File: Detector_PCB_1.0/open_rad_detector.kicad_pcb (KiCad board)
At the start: 2 copper layers, 48.1 x 120.3 mm, 23 parts, among them IC1 LM3914V, J1 Outer_Shield, J2 Electrode, J3 Batt, Q1 FMMT734, Q2 FMMT734, SW1 POWER, SW2 BUZZER, U1 LD1117S50TR_SOT223, U2 MCP6N11

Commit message: Added LEDs
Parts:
- added D10: LED, LEDs:LED_1206, F.Cu at (154.3, 114.6)
- added D11: LED, LEDs:LED_1206, F.Cu at (160.3, 109.1)
- added D3: LED, LEDs:LED_1206, F.Cu at (142.4, 109.1)
- added D4: LED, LEDs:LED_1206, F.Cu at (142.4, 114.6)
- added D5: LED, LEDs:LED_1206, F.Cu at (148.4, 109.1)
- added D6: LED, LEDs:LED_1206, F.Cu at (142.4, 120.2)
- added D7: LED, LEDs:LED_1206, F.Cu at (148.4, 114.6)
- added D8: LED, LEDs:LED_1206, F.Cu at (154.3, 109.1)
- added D9: LED, LEDs:LED_1206, F.Cu at (148.4, 120.2)
- RV1: footprint Potentiometers:Potentiometer_Trimmer_Piher_PT-10v10_Horizontal_Px10.0mm_Py5.0mm_MountLS -> Potentiometers:Potentiometer_Trimmer_Piher_PT-10v10_Horizontal_Px10.0mm_Py5.0mm
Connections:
- BZ1 pad 2: GND -> L10
- IC1 pad 1: (no net) -> L1
- IC1 pad 10: (no net) -> Net-(IC1-Pad10)
- IC1 pad 11: (no net) -> +BATT
- IC1 pad 12: (no net) -> L10
- IC1 pad 13: (no net) -> L9
- IC1 pad 14: (no net) -> L8
- IC1 pad 15: (no net) -> L7
- IC1 pad 16: (no net) -> L6
- IC1 pad 17: (no net) -> L5
- IC1 pad 18: (no net) -> L4
- IC1 pad 19: (no net) -> L3
- IC1 pad 2: (no net) -> GND
- IC1 pad 20: (no net) -> L2
- IC1 pad 3: (no net) -> +BATT
- IC1 pad 4: (no net) -> GND
- IC1 pad 6: (no net) -> Net-(IC1-Pad6)
- IC1 pad 7: (no net) -> Net-(IC1-Pad7)
- IC1 pad 8: (no net) -> Net-(IC1-Pad8)
- IC1 pad 9: (no net) -> Net-(IC1-Pad9)
- J3 pad 1: GND -> Net-(J3-Pad1)
- Q2 pad 1: (no net) -> Net-(Q2-Pad1)
- SW1 pad 1: Net-(J3-Pad2) -> Net-(SW1-Pad1)
- SW2 pad 2: Net-(SW2-Pad2) -> +BATT
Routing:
- net Net-(J3-Pad2): track 43.6 -> 39.2 mm
- net Net-(SW2-Pad2): track 0.65 -> 0.00 mm
- net +BATT: track 122.9 -> 123.6 mm

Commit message: Work in the new version
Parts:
- removed D1: LED, LEDs:LED_1206
- added C5: 10u, Capacitors_SMD:C_1206, F.Cu at (107.4, 147.8)
- added L1: 33u, Inductors_NEOSID:Neosid_Inductor_SM-NE29_SMD1008, F.Cu at (106.4, 151.9)
- added R6: LMR2, Resistors_SMD:R_0805, F.Cu at (117.9, 154.2)
- R4: value R_LED -> LMR1
- moved D8 69.1 mm to (90.0, 134.2), turned to 90 degrees
- moved D5 68.2 mm to (85.0, 134.2), turned to 90 degrees
- moved D3 67.3 mm to (80.0, 134.2), turned to 90 degrees
- moved D10 62.5 mm to (95.0, 134.2), turned to 90 degrees
- moved D11 51.9 mm to (114.9, 134.2), turned to 90 degrees
- moved D4 46.8 mm to (99.9, 134.2), turned to 90 degrees
- moved D9 40.9 mm to (109.9, 134.2), turned to 90 degrees
- moved D6 40.0 mm to (104.9, 134.2), turned to 90 degrees
- moved D7 34.6 mm to (119.9, 134.2), turned to 90 degrees
- moved IC1 24.8 mm to (114.8, 145.0), turned to 90 degrees
- moved R4 23.3 mm to (117.9, 151.9), turned to 0 degrees
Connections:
- D10 pad 2: +BATT -> +12V
- D11 pad 2: +BATT -> +12V
- D3 pad 2: +BATT -> +12V
- D4 pad 2: +BATT -> +12V
- D5 pad 2: +BATT -> +12V
- D6 pad 2: +BATT -> +12V
- D7 pad 2: +BATT -> +12V
- D8 pad 2: +BATT -> +12V
- D9 pad 2: +BATT -> +12V
- IC1 pad 11: +BATT -> +12V
- IC1 pad 3: +BATT -> +12V
- IC1 pad 8: Net-(IC1-Pad8) -> Net-(IC1-Pad6)
- J3 pad 1: Net-(J3-Pad1) -> GND
- R4 pad 1: Net-(D1-Pad1) -> Net-(IC1-Pad6)
- R4 pad 2: GND -> Net-(IC1-Pad10)
- SW1 pad 1: Net-(SW1-Pad1) -> Net-(J3-Pad2)
- SW2 pad 2: +BATT -> +12V
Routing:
- net +12V: track 0.00 -> 85.1 mm, vias 0 -> 4
- net +5V: track 6.96 -> 72.9 mm
- net L10: track 0.00 -> 39.9 mm, vias 0 -> 1
- net L1: track 0.00 -> 35.2 mm
- net L2: track 0.00 -> 29.6 mm
- net +BATT: track 123.6 -> 148.5 mm
- net L3: track 0.00 -> 24.4 mm
- net L5: track 0.00 -> 23.2 mm
- net L4: track 0.00 -> 21.8 mm
- net v_out: track 13.9 -> 34.5 mm, vias 0 -> 2
- net L6: track 0.00 -> 12.7 mm
- net Net-(IC1-Pad10): track 0.00 -> 9.57 mm
- net L7: track 0.00 -> 9.01 mm
- net Net-(IC1-Pad6): track 0.00 -> 7.04 mm
- net L9: track 0.00 -> 7.03 mm
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
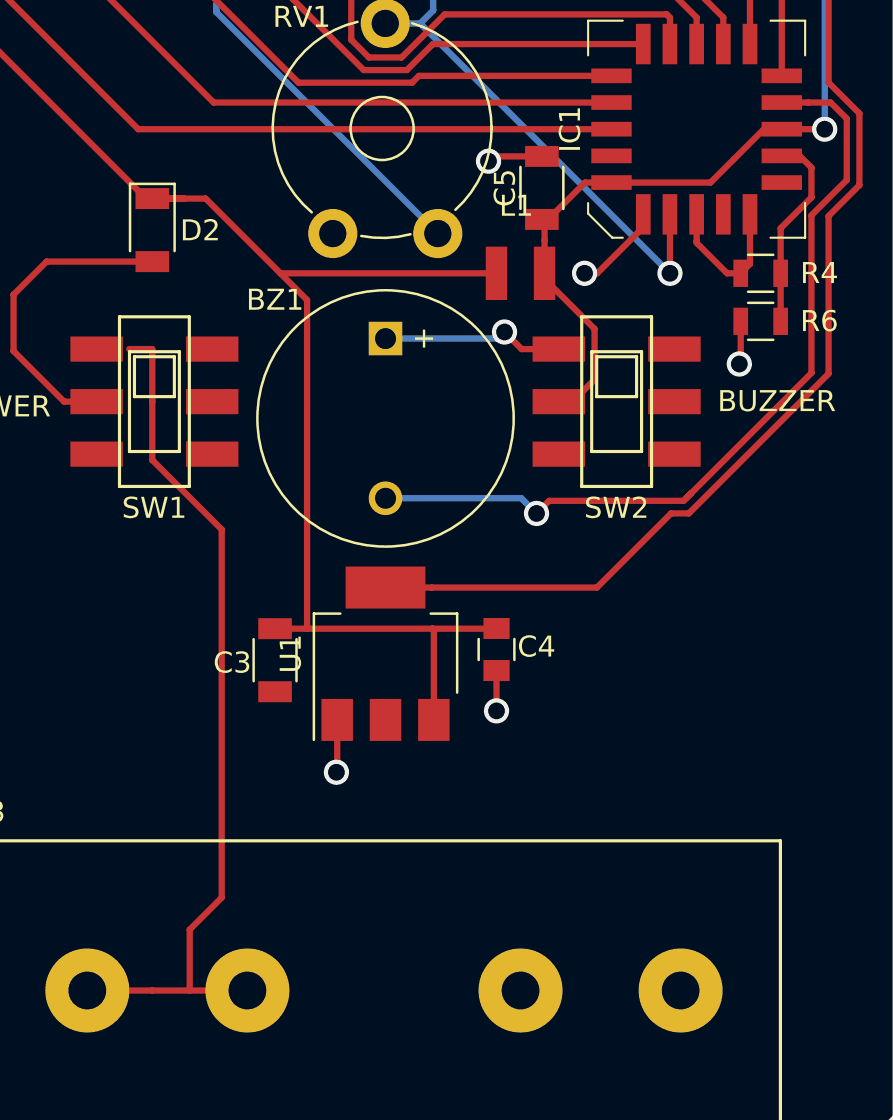
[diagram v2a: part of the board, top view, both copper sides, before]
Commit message: Support latest KiCad version
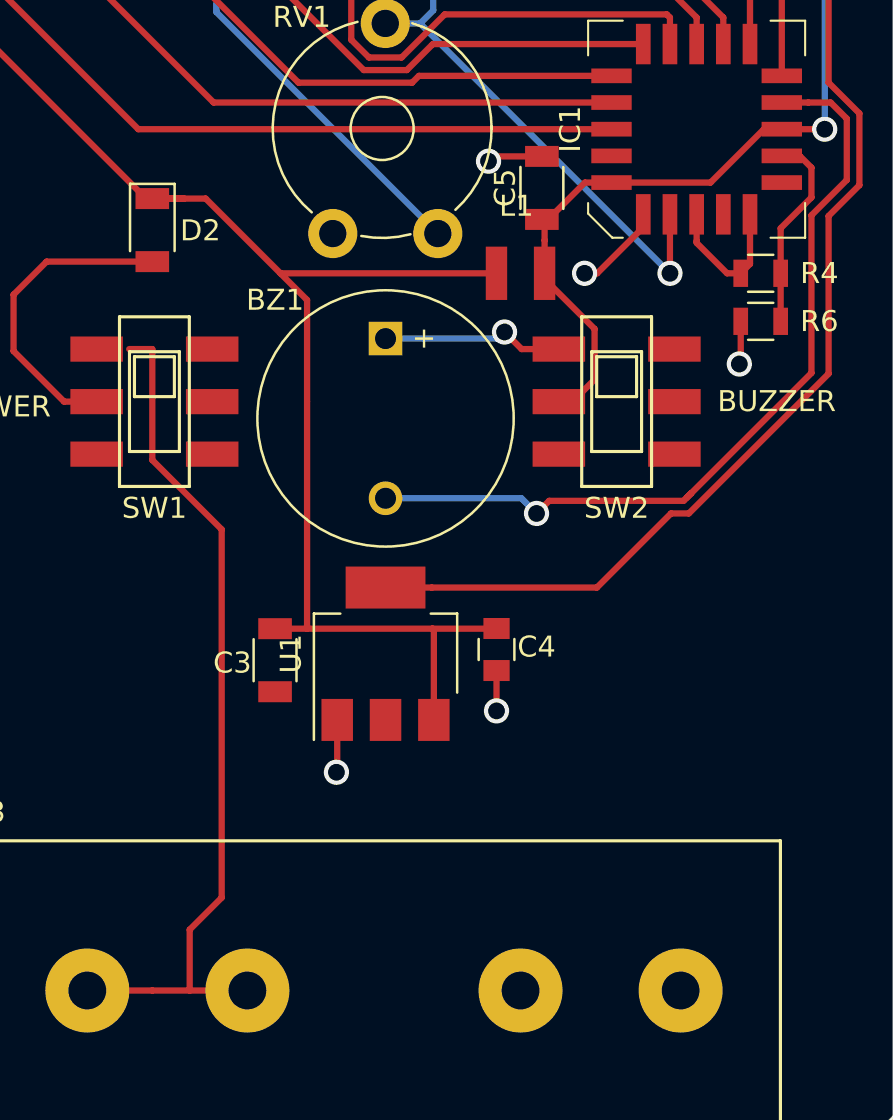
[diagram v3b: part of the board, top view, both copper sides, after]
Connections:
- IC1 pad 7: Net-(IC1-Pad7) -> (no net)
- IC1 pad 9: Net-(IC1-Pad9) -> (no net)
- Q2 pad 1: Net-(Q2-Pad1) -> (no net)

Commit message: Added BOM and Gerbers for V1.0
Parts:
- R5: value 10M -> Rtune
- moved J3 28.2 mm to (85.8, 186.0), turned to 0 degrees
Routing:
- net Net-(J3-Pad2): track 41.2 -> 50.3 mm
- net L5: track 23.2 -> 17.1 mm
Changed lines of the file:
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@@
   (general
     (links 111)
-    (no_connects 11)
+    (no_connects 10)
     (area 75.997999 75.870999 124.281001 196.290001)
     (thickness 1.6)
     (drawings 8)
-    (tracks 293)
+    (tracks 288)
     (zones 0)
     (modules 34)
@@
     (add_net v_rad)
   )
+  (module A23_battery:A23_battery (layer F.Cu)
+    (at 85.806 186.029)
+    (fp_text reference J3 (at 32.766 8.483) (layer F.SilkS)
+      (effects (font (size 1 1) (thickness 0.15)))
+    )
+    (fp_text value Batt (at 4.75 -3.8) (layer F.Fab)
+      (effects (font (size 1 1) (thickness 0.15)))
+    )
+    (fp_line (start -4.75 7.125) (end -4.75 -7.125) (layer F.SilkS) (width 0.15))
+    (fp_line (start 33.25 7.125) (end -4.75 7.125) (layer F.SilkS) (width 0.15))
+    (fp_line (start 33.25 -7.125) (end 33.25 7.125) (layer F.SilkS) (width 0.15))
+    (fp_line (start -4.75 -7.125) (end 33.25 -7.125) (layer F.SilkS) (width 0.15))
+    (pad 1 thru_hole circle (at 7.62 0) (size 4 4) (drill 1.8) (layers *.Cu *.Mask)
+      (net 3 GND))
+    (pad 1 thru_hole circle (at 0 0) (size 4 4) (drill 1.8) (layers *.Cu *.Mask)
+      (net 3 GND))
+    (pad 2 thru_hole circle (at 20.62 0) (size 4 4) (drill 1.8) (layers *.Cu *.Mask)
+      (net 6 "Net-(J3-Pad2)"))
+    (pad 2 thru_hole circle (at 28.24 0) (size 4 4) (drill 1.8) (layers *.Cu *.Mask)
+      (net 6 "Net-(J3-Pad2)"))
+  )
   (module Potentiometers:Potentiometer_Trimmer_Piher_PT-10v10_Horizontal_Px10.0mm_Py5.0mm (layer F.Cu)
     (at 102.489 150 90)
@@
       (rotate (xyz 0 0 180))
     )
-  )
-  (module A23_battery:A23_battery (layer F.Cu)
-    (at 114.046 186.029 180)
-    (fp_text reference J3 (at 32.766 8.483 180) (layer F.SilkS)
-      (effects (font (size 1 1) (thickness 0.15)))
-    )
-    (fp_text value Batt (at 4.75 -3.8 180) (layer F.Fab)
-      (effects (font (size 1 1) (thickness 0.15)))
-    )
-    (fp_line (start -4.75 7.125) (end -4.75 -7.125) (layer F.SilkS) (width 0.15))
-    (fp_line (start 33.25 7.125) (end -4.75 7.125) (layer F.SilkS) (width 0.15))
-    (fp_line (start 33.25 -7.125) (end 33.25 7.125) (layer F.SilkS) (width 0.15))
-    (fp_line (start -4.75 -7.125) (end 33.25 -7.125) (layer F.SilkS) (width 0.15))
-    (pad 1 thru_hole circle (at 7.62 0 180) (size 4 4) (drill 1.8) (layers *.Cu *.Mask)
-      (net 3 GND))
-    (pad 1 thru_hole circle (at 0 0 180) (size 4 4) (drill 1.8) (layers *.Cu *.Mask)
-      (net 3 GND))
-    (pad 2 thru_hole circle (at 20.62 0 180) (size 4 4) (drill 1.8) (layers *.Cu *.Mask)
-      (net 6 "Net-(J3-Pad2)"))
-    (pad 2 thru_hole circle (at 28.24 0 180) (size 4 4) (drill 1.8) (layers *.Cu *.Mask)
-      (net 6 "Net-(J3-Pad2)"))
   )
   (module Capacitors_SMD:C_1206 (layer F.Cu)
@@
       (effects (font (size 1 1) (thickness 0.15)))
     )
-    (fp_text value 10M (at 2.98992 0.7112 360) (layer F.Fab)
+    (fp_text value Rtune (at 2.98992 0.7112 360) (layer F.Fab)
       (effects (font (size 1 1) (thickness 0.15)))
     )
@@
   (segment (start 97.775 129.032) (end 97.3 129.032) (width 0.3) (layer F.Cu) (net 5) (status 30))
   (segment (start 101.854 107.315) (end 101.854 105.648) (width 0.3) (layer F.Cu) (net 5) (status 30))
-  (segment (start 90.678 183.134) (end 92.202 181.61) (width 0.3) (layer F.Cu) (net 6))
-  (segment (start 90.678 186.029) (end 90.678 183.134) (width 0.3) (layer F.Cu) (net 6))
-  (segment (start 92.202 181.61) (end 92.202 164.084) (width 0.3) (layer F.Cu) (net 6))
+  (segment (start 102.6535 186.029) (end 92.202 175.5775) (width 0.3) (layer F.Cu) (net 6))
+  (segment (start 92.202 175.5775) (end 92.202 164.084) (width 0.3) (layer F.Cu) (net 6))
+  (segment (start 106.426 186.029) (end 102.6535 186.029) (width 0.3) (layer F.Cu) (net 6))
+  (segment (start 114.046 186.029) (end 106.426 186.029) (width 0.3) (layer F.Cu) (net 6))
+  (segment (start 87.8 155.5) (end 86.25 155.5) (width 0.3) (layer F.Cu) (net 6))
   (segment (start 92.202 164.084) (end 88.9 160.782) (width 0.3) (layer F.Cu) (net 6))
   (segment (start 88.9 160.782) (end 88.9 155.5) (width 0.3) (layer F.Cu) (net 6))
   (segment (start 88.9 155.5) (end 87.8 155.5) (width 0.3) (layer F.Cu) (net 6))
-  (segment (start 93.426 186.029) (end 90.678 186.029) (width 0.3) (layer F.Cu) (net 6))
-  (segment (start 85.806 186.029) (end 88.9 186.029) (width 0.3) (layer F.Cu) (net 6))
-  (segment (start 88.9 186.029) (end 90.678 186.029) (width 0.3) (layer F.Cu) (net 6))
   (segment (start 102.87 137.414) (end 102.270001 138.013999) (width 0.3) (layer B.Cu) (net 7))
   (segment (start 102.270001 138.013999) (end 102.270001 139.375999) (width 0.3) (layer B.Cu) (net 7))
@@
   (segment (start 88.232 145.034) (end 80.01 136.812) (width 0.3) (layer F.Cu) (net 14))
   (segment (start 80.01 136.812) (end 80.01 135.762) (width 0.3) (layer F.Cu) (net 14) (status 20))
-  (segment (start 102.817603 139.568999) (end 100.766601 141.620001) (width 0.3) (layer F.Cu) (net 15))
-  (segment (start 98.368999 138.520001) (end 99.949 136.94) (width 0.3) (layer F.Cu) (net 15))
-  (segment (start 113.538 140.9815) (end 113.538 139.719) (width 0.3) (layer F.Cu) (net 15) (status 10))
+  (segment (start 113.538 140.9815) (end 113.538 139.719) (width 0.3) (layer F.Cu) (net 15))
   (segment (start 113.538 139.719) (end 113.387999 139.568999) (width 0.3) (layer F.Cu) (net 15))
-  (segment (start 113.387999 139.568999) (end 102.817603 139.568999) (width 0.3) (layer F.Cu) (net 15))
-  (segment (start 100.766601 141.620001) (end 99.211399 141.620001) (width 0.3) (layer F.Cu) (net 15))
-  (segment (start 99.949 136.94) (end 99.949 135.89) (width 0.3) (layer F.Cu) (net 15) (status 20))
-  (segment (start 99.211399 141.620001) (end 98.368999 140.777601) (width 0.3) (layer F.Cu) (net 15))
-  (segment (start 98.368999 140.777601) (end 98.368999 138.520001) (width 0.3) (layer F.Cu) (net 15))
+  (segment (start 113.387999 139.568999) (end 102.577999 139.568999) (width 0.3) (layer F.Cu) (net 15))
+  (segment (start 102.577999 139.568999) (end 99.949 136.94) (width 0.3) (layer F.Cu) (net 15))
+  (segment (start 99.949 136.94) (end 99.949 135.89) (width 0.3) (layer F.Cu) (net 15))
   (segment (start 110.7555 143.764) (end 91.81875 143.764) (width 0.3) (layer F.Cu) (net 16) (status 10))
   (segment (start 91.81875 143.764) (end 84.99475 136.94) (width 0.3) (layer F.Cu) (net 16))
@@
     (polygon
       (pts
-        (xy 98.044 193.548) (xy 80.391 193.548) (xy 80.391 178.562) (xy 98.044 178.562)
+        (xy 118.5545 193.548) (xy 100.9015 193.548) (xy 100.9015 178.562) (xy 118.5545 178.562)
       )
     )
@@
     (polygon
       (pts
-        (xy 80.518 178.689) (xy 97.917 178.689) (xy 97.917 193.421) (xy 80.518 193.421)
+        (xy 101.0285 178.689) (xy 118.4275 178.689) (xy 118.4275 193.421) (xy 101.0285 193.421)
       )
     )
